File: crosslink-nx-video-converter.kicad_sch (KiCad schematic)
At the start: 0 parts

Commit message: Added 3.3V and 1V0_Power SMPSs
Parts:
- added C? (x2): C_10u_0603, antmicro-footprints:0603-cap, symbol antmicroCapacitors0603:C_10u_0603
- added C? (x8): C_22u_0805, antmicro-footprints:0805-cap, symbol antmicroCapacitorsmisc:C_22u_0805
- added C? (x2): C_100n_0603, antmicro-footprints:0603-cap, symbol antmicroCapacitors0603:C_100n_0603
- added L?: DJNR5020-3R3-S, crosslink-nx-video-converter:L_4.9x4.9mm, symbol crosslink-nx-video-converter:DJNR5020-3R3-S
- added L?: DJNR6028-1R5-S, crosslink-nx-video-converter:L_6x6mm-, symbol crosslink-nx-video-converter:DJNR6028-1R5-S
- added R?: R_10k_1%_0603, antmicro-footprints:0603-res, symbol crosslink-nx-video-converter:R_10k_1%_0603
- added R? (x4): R_0R_0805, antmicro-footprints:0805-res, symbol antmicroResistorsmisc:R_0R_0805
- added R?: R_3k01_1%_0603, antmicro-footprints:0603-res, symbol crosslink-nx-video-converter:R_3k01_1%_0603
- added R?: R_33k_0603, antmicro-footprints:0603-res, symbol antmicroResistors0603:R_33k_0603
- added R?: R_10k_0603, antmicro-footprints:0603-res, symbol antmicroResistors0603:R_10k_0603
- added U? (x2): AP62301WU-7, antmicro-footprints:TSOT23-6, symbol antmicroDCDCConverters:AP62301WU-7
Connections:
- new net: R?.1, R?.2, U?.4 (FB)
- new net: C?.1, C?.1, C?.1, C?.1, L?.2 (P), R?.1, R?.1 (x2)
- new net: C?.1, R?.2, U?.3 (VIN) (x2)
- new net: C?.1, U?.6 (BST) (x2)
- new net: C?.2, L?.1 (P), U?.2 (SW) (x2)
- new net: R?.2, R?.2, U?.4 (FB)
- new net +3V3: R?.2
- new net +5V: R?.1, R?.1
- new net 1V0_Power: R?.2
- new net GND: C?.2, C?.2, C?.2, C?.2, C?.2, C?.2, C?.2, C?.2, C?.2, C?.2, R?.1, R?.2, U?.1 (GND), U?.1 (GND)
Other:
- note added: "1.0A max* 86% eff 10mV est. ripple"
- note added: "2.0A max* 94% eff 60mV est. ripple"

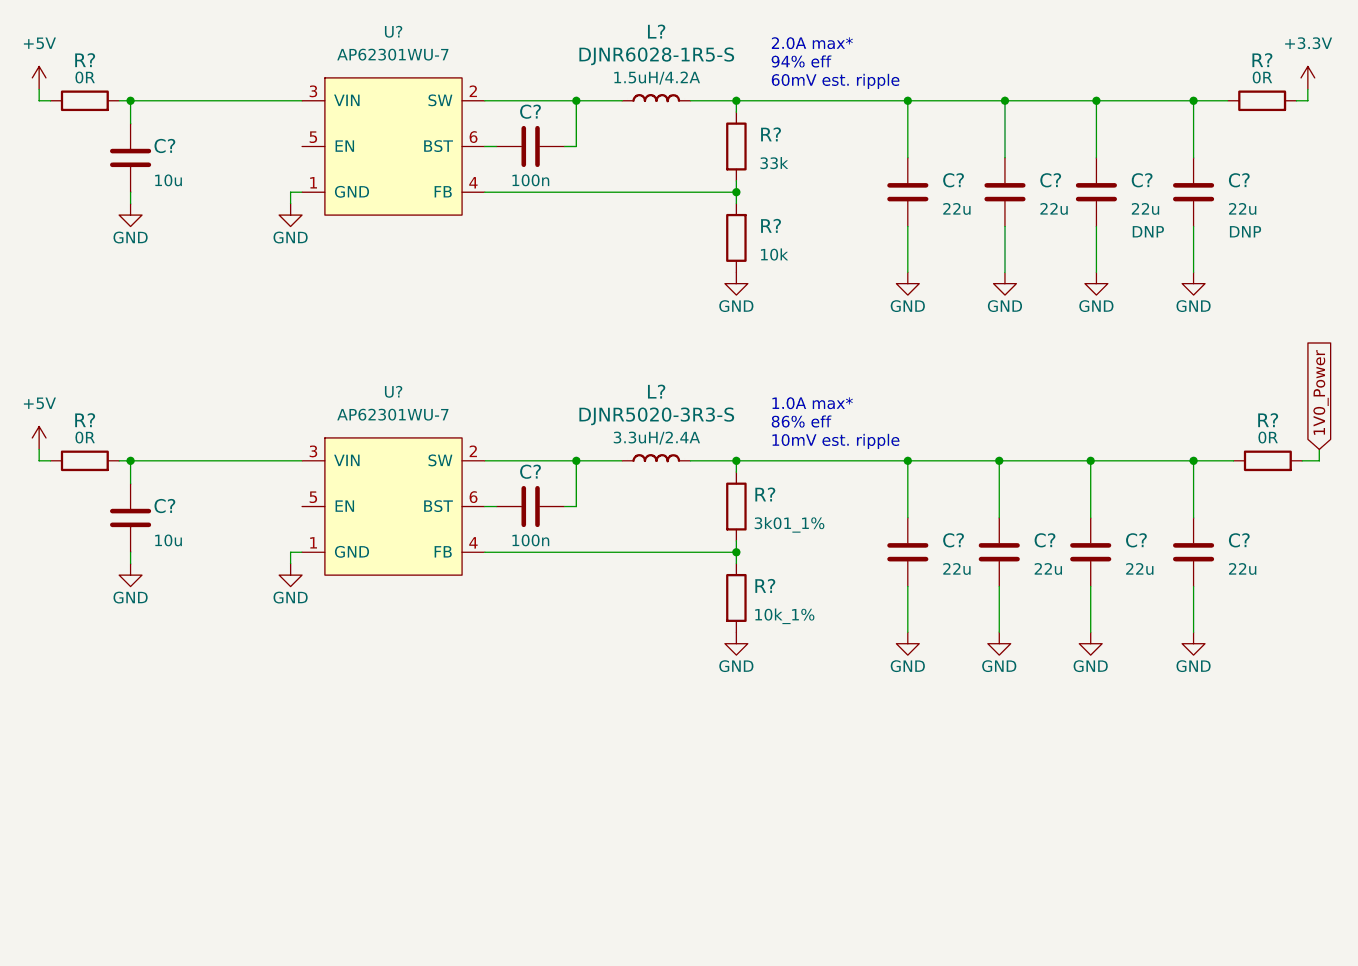
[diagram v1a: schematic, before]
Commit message: Created hierarchy
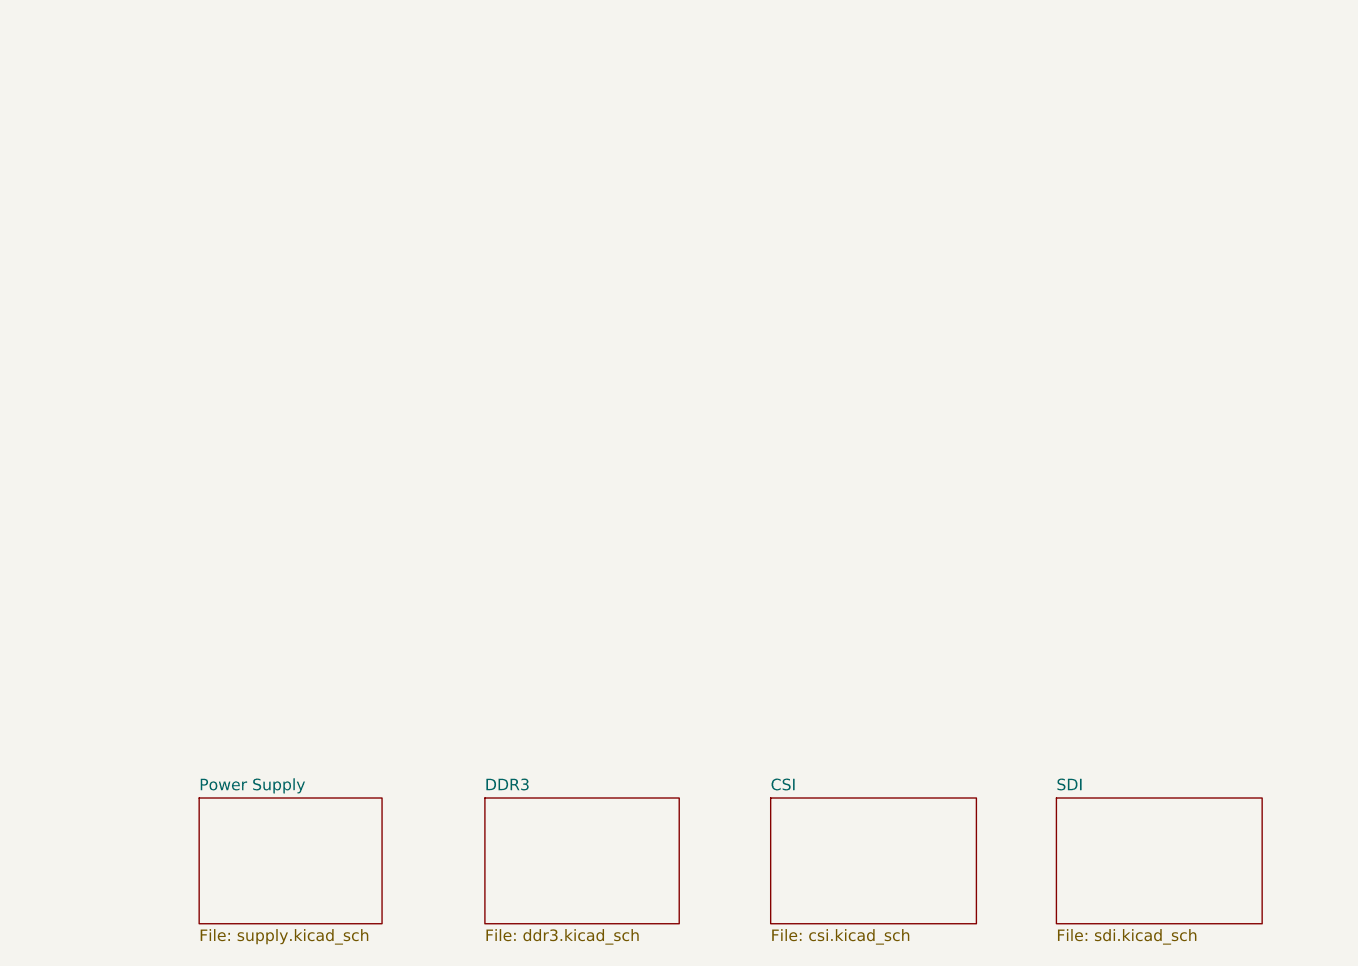
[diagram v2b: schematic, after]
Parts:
- removed C? (x2): C_10u_0603, antmicro-footprints:0603-cap, symbol antmicroCapacitors0603:C_10u_0603
- removed C? (x8): C_22u_0805, antmicro-footprints:0805-cap, symbol antmicroCapacitorsmisc:C_22u_0805
- removed C? (x2): C_100n_0603, antmicro-footprints:0603-cap, symbol antmicroCapacitors0603:C_100n_0603
- removed L?: DJNR5020-3R3-S, crosslink-nx-video-converter:L_4.9x4.9mm, symbol crosslink-nx-video-converter:DJNR5020-3R3-S
- removed L?: DJNR6028-1R5-S, crosslink-nx-video-converter:L_6x6mm-, symbol crosslink-nx-video-converter:DJNR6028-1R5-S
- removed R?: R_10k_1%_0603, antmicro-footprints:0603-res, symbol crosslink-nx-video-converter:R_10k_1%_0603
- removed R? (x4): R_0R_0805, antmicro-footprints:0805-res, symbol antmicroResistorsmisc:R_0R_0805
- removed R?: R_3k01_1%_0603, antmicro-footprints:0603-res, symbol crosslink-nx-video-converter:R_3k01_1%_0603
- removed R?: R_33k_0603, antmicro-footprints:0603-res, symbol antmicroResistors0603:R_33k_0603
- removed R?: R_10k_0603, antmicro-footprints:0603-res, symbol antmicroResistors0603:R_10k_0603
- removed U? (x2): AP62301WU-7, antmicro-footprints:TSOT23-6, symbol antmicroDCDCConverters:AP62301WU-7
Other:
- added sheet CSI (csi.kicad_sch)
- added sheet DDR3 (ddr3.kicad_sch)
- added sheet Power Supply (supply.kicad_sch)
- added sheet SDI (sdi.kicad_sch)
- note removed: "1.0A max* 86% eff 10mV est. ripple"
- note removed: "2.0A max* 94% eff 60mV est. ripple"
